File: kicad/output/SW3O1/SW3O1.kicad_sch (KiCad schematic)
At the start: 36 parts, among them Q1 NTF2955T1G, Q2 DMN2041L, Q3 DMN2041L, T1 42TL004-RC, U1 SW-32MO, U2 LM358ADT/TLV272IS-13

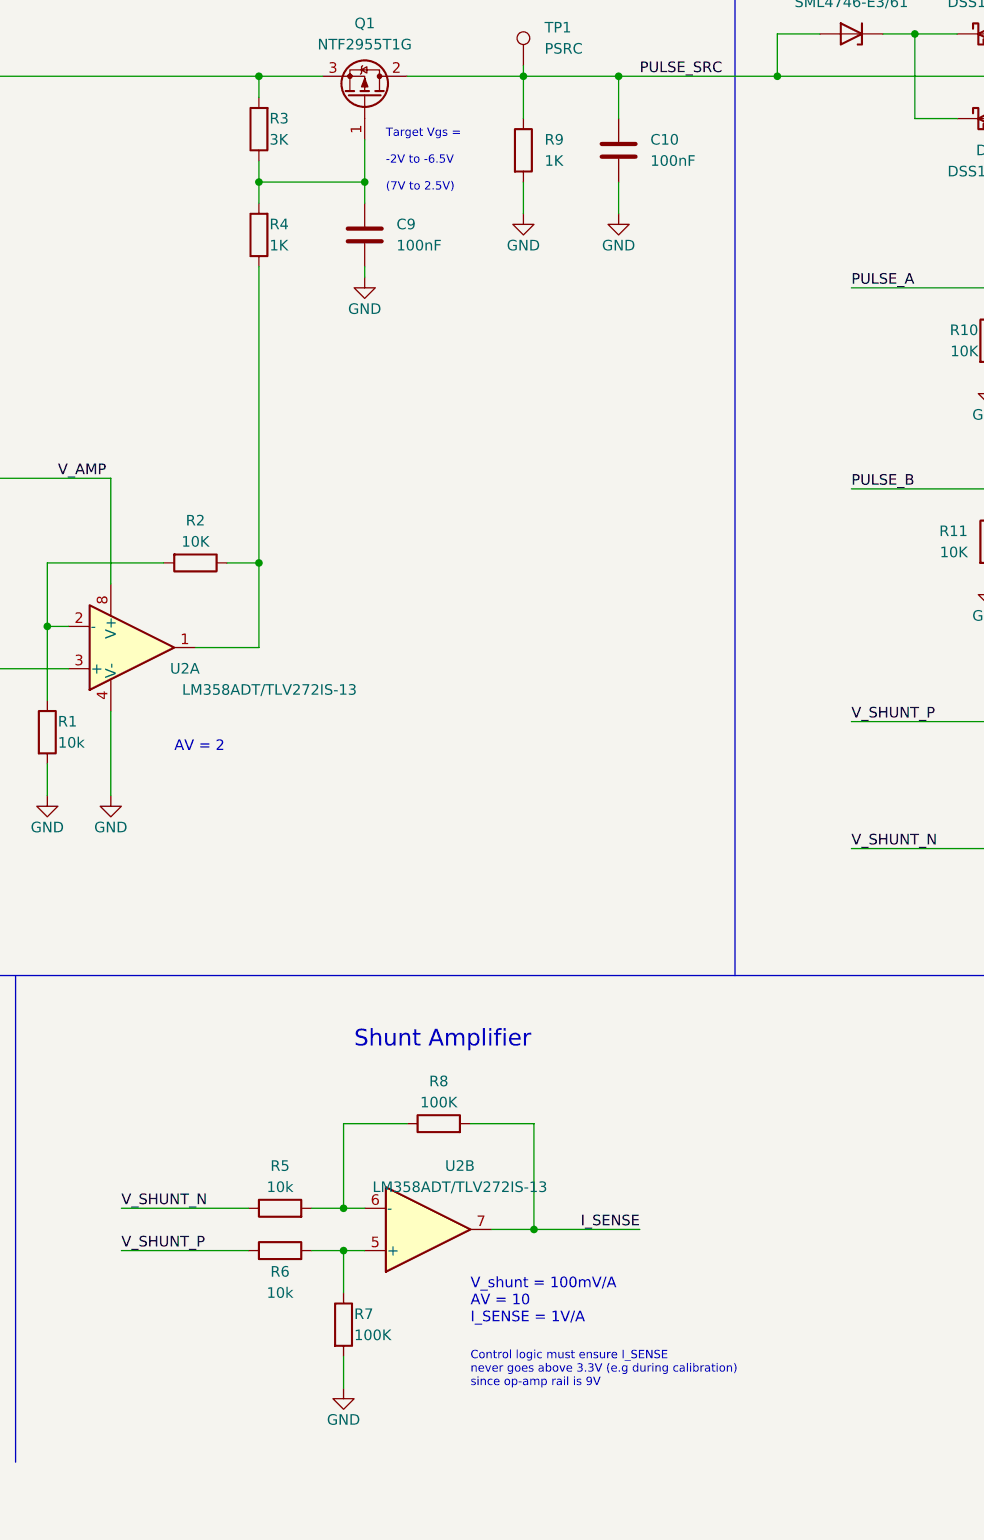
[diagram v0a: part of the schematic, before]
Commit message: use ESP32
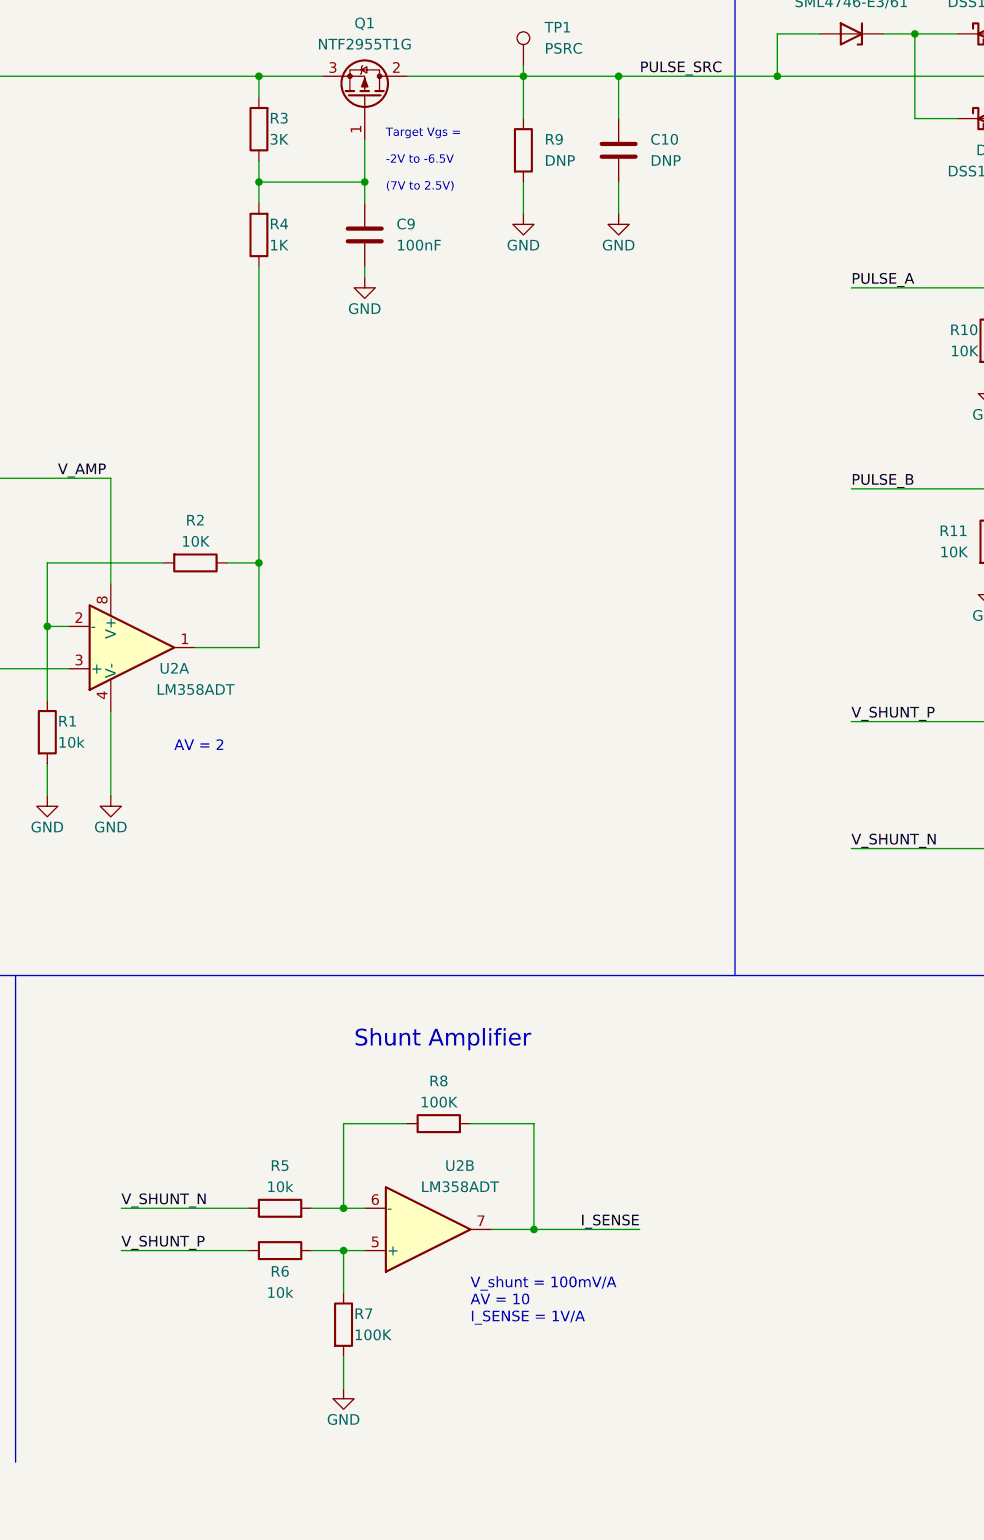
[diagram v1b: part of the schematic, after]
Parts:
- C10: value 100nF -> DNP; now left out of the parts list
- R9: value 1K -> DNP; now left out of the parts list
- TP1: now left out of the parts list
- U2: value LM358ADT/TLV272IS-13 -> LM358ADT; MPN TLV272IS-13 -> LM358ADT
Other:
- note removed: "Control logic must ensure I_SENSE never goes above 3.3V (e.g during calibration) since op-amp rail is 9V"
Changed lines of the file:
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@@
   (title_block
     (title "SW3O1")
-    (date "2022-09-29")
+    (date "2022-11-04")
     (rev "1")
     (company "saawsm")
     (comment 3 "SOT-223 Variant")
-    (comment 4 "A single channel e-stim output module for the SW32x driver board")
+    (comment 4 "A single channel e-stim output module for the SW3X driver board")
   )
   (junction (at 74.93 80.01) (diameter 0) (color 0 0 0 0)
@@
   (text "3.3V logic" (at 41.91 189.23 0)
     (effects (font (size 1.27 1.27)) (justify left bottom))
-  )
-  (text "Control logic must ensure I_SENSE\nnever goes above 3.3V (e.g during calibration)\nsince op-amp rail is 9V"
-    (at 138.43 189.23 0)
-    (effects (font (size 1 1)) (justify left bottom))
   )
   (label "OUTA" (at 69.85 168.91 180)
@@
   )
   (symbol (lib_id "Device:R") (at 144.78 40.64 0) (unit 1)
-    (in_bom yes) (on_board yes) (fields_autoplaced)
+    (in_bom no) (on_board yes) (fields_autoplaced)
     (property "Reference" "R9" (id 0) (at 147.32 39.3699 0)
       (effects (font (size 1.27 1.27)) (justify left))
     )
-    (property "Value" "1K" (id 1) (at 147.32 41.9099 0)
+    (property "Value" "DNP" (id 1) (at 147.32 41.9099 0)
       (effects (font (size 1.27 1.27)) (justify left))
     )
@@
   )
   (symbol (lib_id "Connector:TestPoint") (at 144.78 30.48 0) (unit 1)
-    (in_bom yes) (on_board yes) (fields_autoplaced)
+    (in_bom no) (on_board yes) (fields_autoplaced)
     (property "Reference" "TP1" (id 0) (at 147.32 25.9079 0)
       (effects (font (size 1.27 1.27)) (justify left))
@@
       (effects (font (size 1.27 1.27)) (justify left) hide)
     )
-    (property "Value" "LM358ADT/TLV272IS-13" (id 1) (at 96.52 105.41 0)
+    (property "Value" "LM358ADT" (id 1) (at 96.52 105.41 0)
       (effects (font (size 1.27 1.27)) (justify left) hide)
     )
@@
       (effects (font (size 1.27 1.27)) hide)
     )
-    (property "Datasheet" "http://www.ti.com/lit/ds/symlink/lmc6482.pdf" (id 3) (at 97.79 100.33 0)
-      (effects (font (size 1.27 1.27)) hide)
-    )
-    (property "MPN" "TLV272IS-13" (id 4) (at 97.79 100.33 0)
+    (property "Datasheet" "~" (id 3) (at 97.79 100.33 0)
+      (effects (font (size 1.27 1.27)) hide)
+    )
+    (property "MPN" "LM358ADT" (id 4) (at 97.79 100.33 0)
       (effects (font (size 1.27 1.27)) hide)
     )
@@
   )
   (symbol (lib_id "Device:C") (at 156.21 40.64 0) (unit 1)
-    (in_bom yes) (on_board yes) (fields_autoplaced)
+    (in_bom no) (on_board yes) (fields_autoplaced)
     (property "Reference" "C10" (id 0) (at 160.02 39.3699 0)
       (effects (font (size 1.27 1.27)) (justify left))
     )
-    (property "Value" "100nF" (id 1) (at 160.02 41.9099 0)
+    (property "Value" "DNP" (id 1) (at 160.02 41.9099 0)
       (effects (font (size 1.27 1.27)) (justify left))
     )
@@
     (in_bom yes) (on_board yes)
     (property "Reference" "U2" (id 0) (at 137.16 162.56 0))
-    (property "Value" "LM358ADT/TLV272IS-13" (id 1) (at 137.16 165.1 0))
+    (property "Value" "LM358ADT" (id 1) (at 137.16 165.1 0))
     (property "Footprint" "Package_SO:SOIC-8_3.9x4.9mm_P1.27mm" (id 2) (at 133.35 170.18 0)
       (effects (font (size 1.27 1.27)) hide)
     )
-    (property "Datasheet" "http://www.ti.com/lit/ds/symlink/lmc6482.pdf" (id 3) (at 133.35 170.18 0)
-      (effects (font (size 1.27 1.27)) hide)
-    )
-    (property "MPN" "TLV272IS-13" (id 4) (at 133.35 170.18 0)
+    (property "Datasheet" "~" (id 3) (at 133.35 170.18 0)
+      (effects (font (size 1.27 1.27)) hide)
+    )
+    (property "MPN" "LM358ADT" (id 4) (at 133.35 170.18 0)
       (effects (font (size 1.27 1.27)) hide)
     )
@@
   (symbol (lib_id "Amplifier_Operational:LMC6482") (at 97.79 100.33 0) (mirror x) (unit 1)
     (in_bom yes) (on_board yes)
-    (property "Reference" "U2" (id 0) (at 104.14 102.87 0))
-    (property "Value" "LM358ADT/TLV272IS-13" (id 1) (at 114.3 105.41 0))
+    (property "Reference" "U2" (id 0) (at 102.87 102.87 0))
+    (property "Value" "LM358ADT" (id 1) (at 105.41 105.41 0))
     (property "Footprint" "Package_SO:SOIC-8_3.9x4.9mm_P1.27mm" (id 2) (at 97.79 100.33 0)
       (effects (font (size 1.27 1.27)) hide)
     )
-    (property "Datasheet" "http://www.ti.com/lit/ds/symlink/lmc6482.pdf" (id 3) (at 97.79 100.33 0)
-      (effects (font (size 1.27 1.27)) hide)
-    )
-    (property "MPN" "TLV272IS-13" (id 4) (at 97.79 100.33 0)
+    (property "Datasheet" "~" (id 3) (at 97.79 100.33 0)
+      (effects (font (size 1.27 1.27)) hide)
+    )
+    (property "MPN" "LM358ADT" (id 4) (at 97.79 100.33 0)
       (effects (font (size 1.27 1.27)) hide)
     )
@@
     )
     (path "/a739951a-0aa3-41b7-ab13-958ea04b8230"
-      (reference "C10") (unit 1) (value "100nF") (footprint "Capacitor_SMD:C_0603_1608Metric")
+      (reference "C10") (unit 1) (value "DNP") (footprint "Capacitor_SMD:C_0603_1608Metric")
     )
     (path "/10886180-9d78-4ef1-a84c-c9234de41ca6"
@@
     )
     (path "/4d790691-aa8f-43bd-a8b0-4b361c31c272"
-      (reference "R9") (unit 1) (value "1K") (footprint "Resistor_SMD:R_0603_1608Metric")
+      (reference "R9") (unit 1) (value "DNP") (footprint "Resistor_SMD:R_0603_1608Metric")
     )
     (path "/505a33df-d18d-42f5-b21a-0d35edec1115"
@@
     )
     (path "/eff460af-27f8-4045-a685-ff76d21380fa"
-      (reference "U2") (unit 1) (value "LM358ADT/TLV272IS-13") (footprint "Package_SO:SOIC-8_3.9x4.9mm_P1.27mm")
+      (reference "U2") (unit 1) (value "LM358ADT") (footprint "Package_SO:SOIC-8_3.9x4.9mm_P1.27mm")
     )
     (path "/cabe7585-752f-4afc-8c5b-2da697eb1a0c"
-      (reference "U2") (unit 2) (value "LM358ADT/TLV272IS-13") (footprint "Package_SO:SOIC-8_3.9x4.9mm_P1.27mm")
+      (reference "U2") (unit 2) (value "LM358ADT") (footprint "Package_SO:SOIC-8_3.9x4.9mm_P1.27mm")
     )
     (path "/a28fa6f3-7f0b-49c3-aa60-14cbc192acc5"
-      (reference "U2") (unit 3) (value "LM358ADT/TLV272IS-13") (footprint "Package_SO:SOIC-8_3.9x4.9mm_P1.27mm")
-    )
-  )
+      (reference "U2") (unit 3) (value "LM358ADT") (footprint "Package_SO:SOIC-8_3.9x4.9mm_P1.27mm")
+    )
+  )

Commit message: cleanup
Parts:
- removed C10: DNP, Capacitor_SMD:C_0603_1608Metric, symbol Device:C
- removed R9: DNP, Resistor_SMD:R_0603_1608Metric, symbol Device:R
- R3: value 3K -> 2K; MPN RC0603FR-073KL -> RC0603FR-072KL
- renumbered R11 to R10, R12 to R11, R13 to R12, R14 to R13, R10 to R9
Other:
- note added: "Target Vgs = -1.6V to -6V (7.4V to 3V)"
- note removed: "Target Vgs = -2V to -6.5V (7V to 2.5V)"

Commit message: simplify bom - use SS24FL
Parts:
- D2, D3: value DSS14UTR -> SS24FL; LCSC (none) -> C894433; MOUSER (none) -> 512-SS24FL; MPN DSS14U -> SS24FL
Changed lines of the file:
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@@
   (title_block
     (title "SW3O1")
-    (date "2022-11-08")
+    (date "2022-12-23")
     (rev "1")
     (company "saawsm")
@@
   (symbol (lib_id "Transistor_FET:DMN2041L") (at 218.44 81.28 0) (unit 1)
     (in_bom yes) (on_board yes)
-    (property "Reference" "Q2" (id 0) (at 224.79 73.66 0)
-      (effects (font (size 1.27 1.27)) (justify left))
-    )
-    (property "Value" "DMN2041L" (id 1) (at 224.79 76.2 0)
+    (property "Reference" "Q2" (id 0) (at 224.79 80.01 0)
+      (effects (font (size 1.27 1.27)) (justify left))
+    )
+    (property "Value" "DMN2041L" (id 1) (at 224.79 82.55 0)
       (effects (font (size 1.27 1.27)) (justify left))
     )
@@
     (in_bom yes) (on_board yes) (fields_autoplaced)
     (property "Reference" "D3" (id 0) (at 200.3425 40.64 0))
-    (property "Value" "DSS14UTR" (id 1) (at 200.3425 43.18 0))
+    (property "Value" "SS24FL" (id 1) (at 200.3425 43.18 0))
     (property "Footprint" "Diode_SMD:D_SOD-123F" (id 2) (at 200.66 36.83 0)
       (effects (font (size 1.27 1.27)) hide)
@@
       (effects (font (size 1.27 1.27)) hide)
     )
-    (property "MPN" "DSS14U" (id 4) (at 200.66 36.83 0)
+    (property "MPN" "SS24FL" (id 4) (at 200.66 36.83 0)
+      (effects (font (size 1.27 1.27)) hide)
+    )
+    (property "MOUSER" "512-SS24FL" (id 5) (at 200.66 36.83 0)
+      (effects (font (size 1.27 1.27)) hide)
+    )
+    (property "LCSC" "C894433" (id 6) (at 200.66 36.83 0)
       (effects (font (size 1.27 1.27)) hide)
     )
@@
     (in_bom yes) (on_board yes) (fields_autoplaced)
     (property "Reference" "D2" (id 0) (at 200.3425 20.32 0))
-    (property "Value" "DSS14UTR" (id 1) (at 200.3425 22.86 0))
+    (property "Value" "SS24FL" (id 1) (at 200.3425 22.86 0))
     (property "Footprint" "Diode_SMD:D_SOD-123F" (id 2) (at 200.66 26.67 0)
       (effects (font (size 1.27 1.27)) hide)
@@
       (effects (font (size 1.27 1.27)) hide)
     )
-    (property "MPN" "DSS14U" (id 4) (at 200.66 26.67 0)
+    (property "MPN" "SS24FL" (id 4) (at 200.66 26.67 0)
+      (effects (font (size 1.27 1.27)) hide)
+    )
+    (property "LCSC" "C894433" (id 5) (at 200.66 26.67 0)
+      (effects (font (size 1.27 1.27)) hide)
+    )
+    (property "MOUSER" "512-SS24FL" (id 6) (at 200.66 26.67 0)
       (effects (font (size 1.27 1.27)) hide)
     )
@@
     )
     (path "/fb44cdac-4dd3-4941-896e-479910f28a69"
-      (reference "D2") (unit 1) (value "DSS14UTR") (footprint "Diode_SMD:D_SOD-123F")
+      (reference "D2") (unit 1) (value "SS24FL") (footprint "Diode_SMD:D_SOD-123F")
     )
     (path "/4abcd740-c754-47a0-9473-c44600c69288"
-      (reference "D3") (unit 1) (value "DSS14UTR") (footprint "Diode_SMD:D_SOD-123F")
+      (reference "D3") (unit 1) (value "SS24FL") (footprint "Diode_SMD:D_SOD-123F")
     )
     (path "/556b248a-0411-4c59-9fcf-b5ee438fedf7"
